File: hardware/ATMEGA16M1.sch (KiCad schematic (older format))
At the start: 56 parts, among them IC1 ATMEGA16M1-A, IC2 MCP2551-I/SN, J1 PWR, J2 USB, J3 RELAY, J4 RELAY, J5 RELAY, J6 GPIO, J7 AMP/D2A, J8 ADC, J9 CAN, SW1 RESET, U1 NCP1117ST50T3G, U2 FT232RL, U3 RELAY_VO14642AT, U4 RELAY_VO14642AT, U5 RELAY_VO14642AT, X1 16MHz

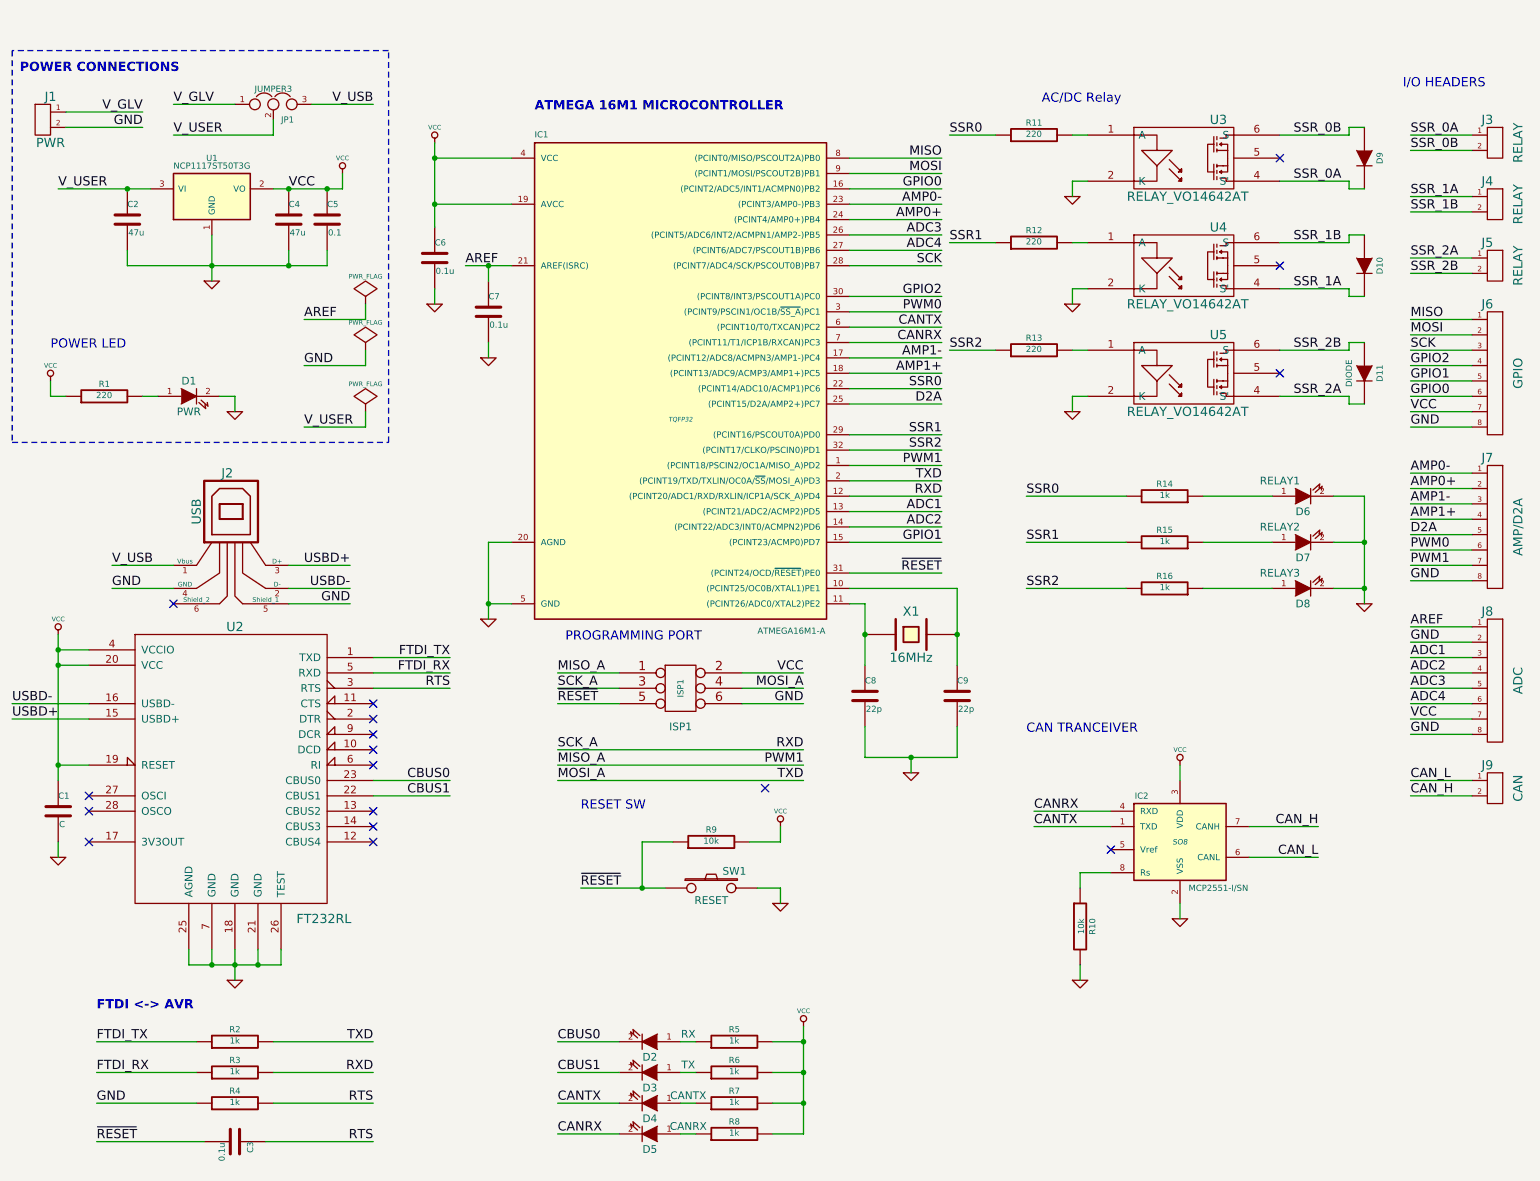
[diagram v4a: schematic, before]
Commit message: BOM added & schematic updated with Digikey P/N's
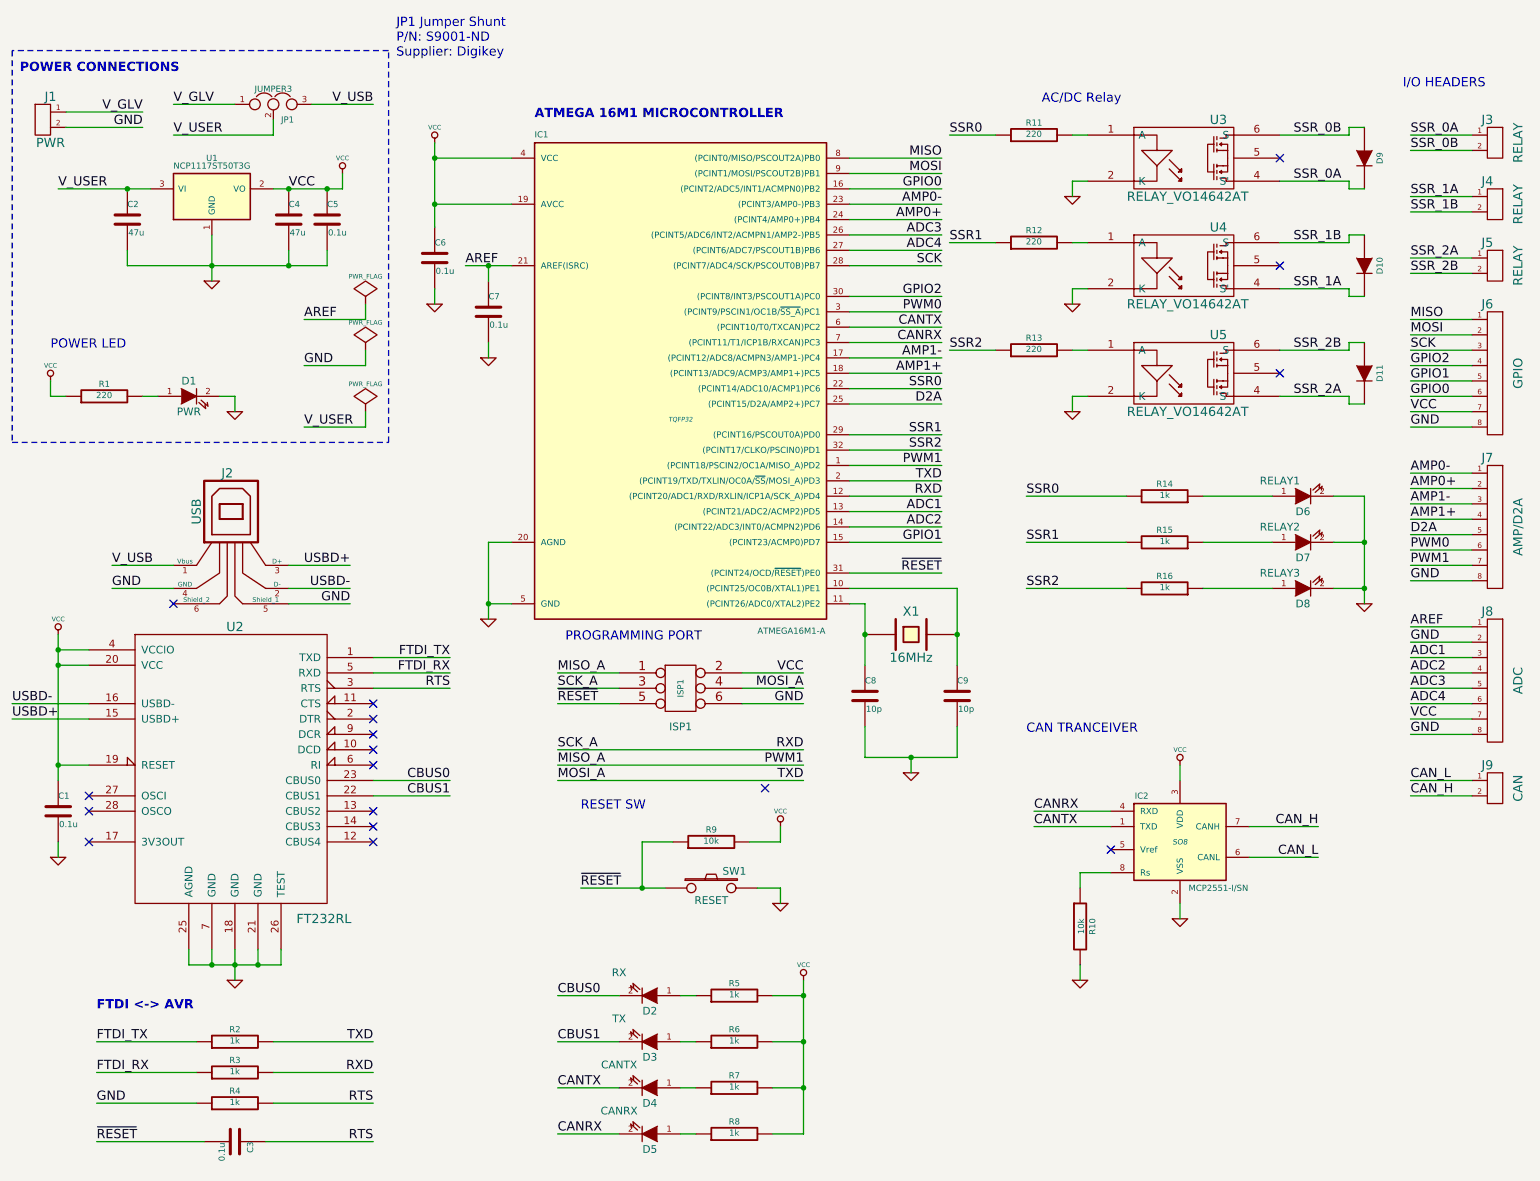
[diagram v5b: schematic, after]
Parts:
- C1: value C -> 0.1u; P/N (none) -> 490-1524-1-ND; Supplier (none) -> Digikey; URL (none) -> http://www.digikey.com/product-detail/en/GRM188R71E104KA01D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
- C2, C4: P/N (none) -> PCE5005CT-ND; Supplier (none) -> Digikey; URL (none) -> http://www.digikey.com/product-detail/en/EEE-FT1E470AR/PCE5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
- C3, C6, C7: P/N (none) -> 490-1524-1-ND; Supplier (none) -> Digikey; URL (none) -> http://www.digikey.com/product-detail/en/GRM188R71E104KA01D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
- C5: value 0.1 -> 0.1u; P/N (none) -> 490-1524-1-ND; Supplier (none) -> Digikey; URL (none) -> http://www.digikey.com/product-detail/en/GRM188R71E104KA01D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
- C8, C9: value 22p -> 10p; P/N (none) -> 490-1403-1-ND; Supplier (none) -> Digikey; URL (none) -> http://www.digikey.com/product-detail/en/GRM1885C1H100JA01D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
- D10, D11, D9: P/N (none) -> SK310A-LTPMSCT-ND; Supplier (none) -> Digikey; URL (none) -> http://www.digikey.com/product-detail/en/SK310A-LTP/SK310A-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
- D2, D5: P/N (none) -> 732-4981-1-ND; Supplier (none) -> Digikey; URL (none) -> http://www.digikey.com/product-detail/en/150060YS75000/732-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
- D3, D4: P/N (none) -> 732-4978-1-ND; Supplier (none) -> Digikey; URL (none) -> http://www.digikey.com/product-detail/en/150060RS75000/732-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
- D6, D7, D8: P/N (none) -> 732-4971-1-ND; Supplier (none) -> Digikey; URL (none) -> http://www.digikey.com/product-detail/en/150060GS75000/732-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
- IC2: P/N (none) -> MCP2551T-E/SNCT-ND; Supplier (none) -> Digikey; URL (none) -> http://www.digikey.com/product-detail/en/MCP2551T-E%2FSN/MC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
- ISP1: P/N (none) -> 3M15451-ND; Supplier (none) -> Digikey; URL (none) -> http://www.digikey.com/product-detail/en/30306-6002HB/3M154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
- J1, J3, J4, J5, J9: P/N (none) -> ED2609-ND; Supplier (none) -> Digikey; URL (none) -> http://www.digikey.com/product-detail/en/OSTTC022162/ED2609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
- J2: P/N (none) -> 609-4613-1-ND; Supplier (none) -> Digikey; URL (none) -> http://www.digikey.com/product-detail/en/10118192-0001LF/60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
- J6, J7, J8: P/N (none) -> ED2615-ND; Supplier (none) -> Digikey; URL (none) -> http://www.digikey.com/product-detail/en/OSTTC082162/ED2615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
- JP1: P/N (none) -> 952-2264-ND; Supplier (none) -> Digikey; URL (none) -> http://www.digikey.com/product-detail/en/M20-9990346/952-22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
- R1, R11, R12, R13: P/N (none) -> RHM220CGCT-ND; Supplier (none) -> Digikey; URL (none) -> http://www.digikey.com/product-detail/en/MCR03ERTJ221/RHM22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
- R10, R9: P/N (none) -> RHM10KCGCT-ND; Supplier (none) -> Digikey; URL (none) -> http://www.digikey.com/product-detail/en/MCR03ERTJ103/RHM10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
- R14, R15, R16, R2, R3, R4, R5, R6, R7, R8: P/N (none) -> RHM1.0KCGCT-ND; Supplier (none) -> Digikey; URL (none) -> http://www.digikey.com/product-detail/en/MCR03ERTJ102/RHM1.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
- SW1: P/N (none) -> 401-1427-1-ND; Supplier (none) -> Digikey; URL (none) -> http://www.digikey.com/product-detail/en/KMR221GLFS/401-142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
- U2: footprint (none) -> ~; P/N (none) -> 768-1007-1-ND; Supplier (none) -> Digikey; URL (none) -> http://www.digikey.com/product-detail/en/FT232RL-REEL/768-1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
- U3: P/N (none) -> VO14642AABCT-ND; Supplier (none) -> Digkey; URL (none) -> http://www.digikey.com/product-detail/en/VO14642AABTR/VO146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
- U4, U5: P/N (none) -> VO14642AABCT-ND; Supplier (none) -> Digikey; URL (none) -> http://www.digikey.com/product-detail/en/VO14642AABTR/VO146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
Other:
- note added: "JP1 Jumper Shunt\nP/N: S9001-ND\nSupplier: Digikey"
- moved on the sheet: D2, D3, D4, R5, R6, R7

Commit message: FTDI <-> ISP issue addressed, dip switch added
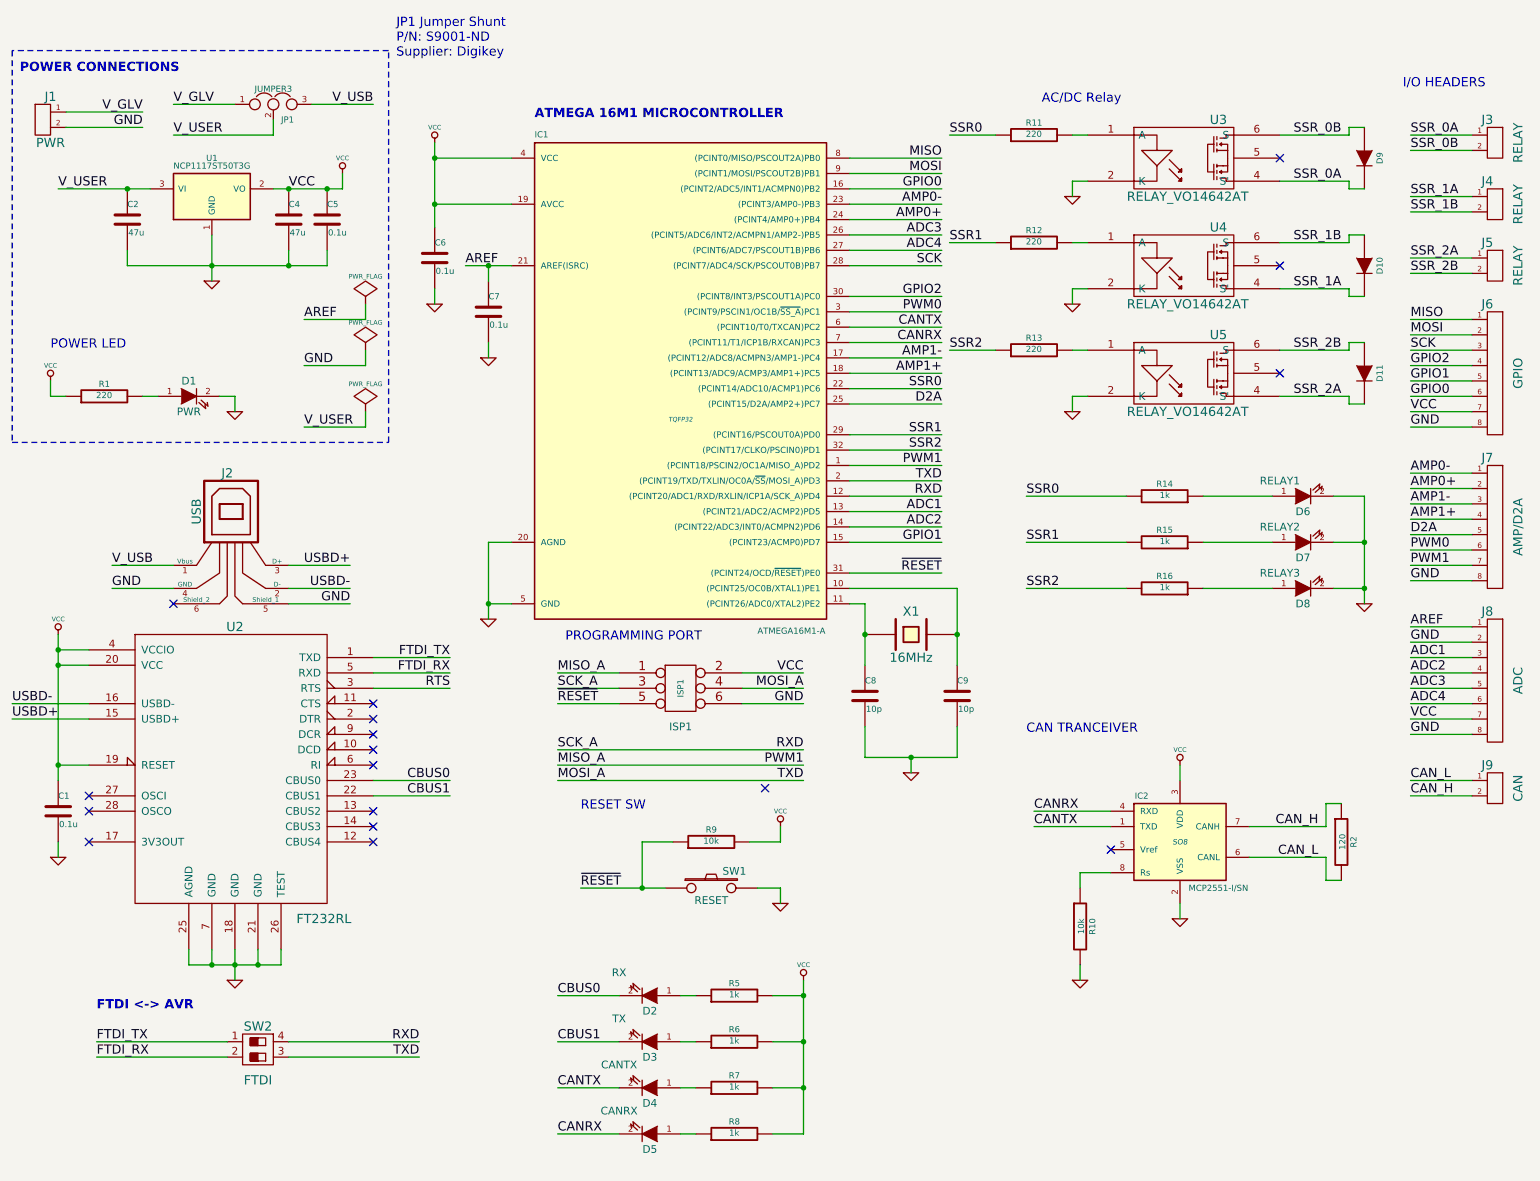
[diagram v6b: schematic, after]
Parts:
- removed C3: 0.1u, ~, symbol C
- removed R3, R4: 1k, ~, symbol R
- added SW2: FTDI, symbol DIPS_02
- R2: value 1k -> 120; P/N RHM1.0KCGCT-ND -> (none); Supplier Digikey -> (none); URL http://www.digikey.com/product-detail/en/MCR03ERTJ102/RHM1.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 -> (none)
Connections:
- net CAN_H: now also R2.1
- net CAN_L: now also R2.2
- net FTDI_RX: now also SW2.2
- net FTDI_TX: now also SW2.1; no longer R2.1
- net MOSI_A: now also SW2.3; no longer R2.2
- net RXD: now also SW2.4
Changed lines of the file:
@@
 LIBS:w_analog
 LIBS:custom
+LIBS:dips-s
 LIBS:ATMEGA16M1-cache
 EELAYER 27 0
@@
 Sheet 1 1
 Title "LFEF CAN Communication Board"
-Date "2 apr 2015"
+Date "11 apr 2015"
 Rev "0"
 Comp "Lafayette College"
@@
 	1    0    0    -1
 $EndComp
-Text Label 2900 7000 2    60   ~ 0
+Text Label 3200 7100 2    60   ~ 0
 TXD
-Text Label 2900 7200 2    60   ~ 0
+Text Label 3200 7000 2    60   ~ 0
 RXD
-$Comp
-L R R2
-U 1 1 54DE18B6
-P 2000 7000
-F 0 "R2" V 2080 7000 40  0000 C CNN
-F 1 "1k" V 2007 7001 40  0000 C CNN
-F 2 "~" V 1930 7000 30  0000 C CNN
-F 3 "~" H 2000 7000 30  0000 C CNN
-F 4 "RHM1.0KCGCT-ND" H 2000 7000 60  0001 C CNN "P/N"
-F 5 "Digikey" H 2000 7000 60  0001 C CNN "Supplier"
-F 6 "http://www.digikey.com/product-detail/en/MCR03ERTJ102/RHM1.0KCGCT-ND/2796495" H 2000 7000 60  0001 C CNN "URL"
-	1    2000 7000
-	0    -1   -1   0
-$EndComp
-$Comp
-L R R3
-U 1 1 54DE18C3
-P 2000 7200
-F 0 "R3" V 2080 7200 40  0000 C CNN
-F 1 "1k" V 2007 7201 40  0000 C CNN
-F 2 "~" V 1930 7200 30  0000 C CNN
-F 3 "~" H 2000 7200 30  0000 C CNN
-F 4 "RHM1.0KCGCT-ND" H 2000 7200 60  0001 C CNN "P/N"
-F 5 "Digikey" H 2000 7200 60  0001 C CNN "Supplier"
-F 6 "http://www.digikey.com/product-detail/en/MCR03ERTJ102/RHM1.0KCGCT-ND/2796495" H 2000 7200 60  0001 C CNN "URL"
-	1    2000 7200
-	0    -1   -1   0
-$EndComp
 Text Label 1100 7000 0    60   ~ 0
 FTDI_TX
-Text Label 1100 7200 0    60   ~ 0
+Text Label 1100 7100 0    60   ~ 0
 FTDI_RX
-Text Label 2900 7650 2    60   ~ 0
-RTS
-Text Label 1100 7650 0    60   ~ 0
-~RESET
-$Comp
-L C C3
-U 1 1 54DE18FF
-P 2000 7650
-F 0 "C3" H 2000 7750 40  0000 L CNN
-F 1 "0.1u" H 2006 7565 40  0000 L CNN
-F 2 "~" H 2038 7500 30  0000 C CNN
-F 3 "~" H 2000 7650 60  0000 C CNN
-F 4 "490-1524-1-ND" H 2000 7650 60  0001 C CNN "P/N"
-F 5 "Digikey" H 2000 7650 60  0001 C CNN "Supplier"
-F 6 "http://www.digikey.com/product-detail/en/GRM188R71E104KA01D/490-1524-1-ND/587865" H 2000 7650 60  0001 C CNN "URL"
-	1    2000 7650
-	0    1    1    0
-$EndComp
 $Comp
 L C C5
@@
 Text Notes 3950 1000 0    60   ~ 12
 ATMEGA 16M1 MICROCONTROLLER
-Text Label 2900 7400 2    60   ~ 0
-RTS
-$Comp
-L R R4
-U 1 1 54DE1D1D
-P 2000 7400
-F 0 "R4" V 2080 7400 40  0000 C CNN
-F 1 "1k" V 2007 7401 40  0000 C CNN
-F 2 "~" V 1930 7400 30  0000 C CNN
-F 3 "~" H 2000 7400 30  0000 C CNN
-F 4 "RHM1.0KCGCT-ND" H 2000 7400 60  0001 C CNN "P/N"
-F 5 "Digikey" H 2000 7400 60  0001 C CNN "Supplier"
-F 6 "http://www.digikey.com/product-detail/en/MCR03ERTJ102/RHM1.0KCGCT-ND/2796495" H 2000 7400 60  0001 C CNN "URL"
-	1    2000 7400
-	0    -1   -1   0
-$EndComp
-Text Label 1100 7400 0    60   ~ 0
-GND
 $Comp
 L MCP2551-I/SN IC2
@@
 	3800 4150 3650 4150
 Wire Wire Line
-	3650 3750 3650 4150
-Wire Wire Line
-	3650 4150 3650 4250
+	3650 3750 3650 4250
 Wire Wire Line
 	3800 1250 3300 1250
 Wire Wire Line
-	3300 1150 3300 1250
-Wire Wire Line
-	3300 1250 3300 1550
-Wire Wire Line
-	3300 1550 3300 1700
+	3300 1150 3300 1700
 Wire Wire Line
 	6000 4150 6100 4150
 Wire Wire Line
-	6100 4150 6100 4350
-Wire Wire Line
-	6100 4350 6100 4550
+	6100 4150 6100 4550
 Wire Wire Line
 	6000 4050 6700 4050
 Wire Wire Line
-	6700 4050 6700 4350
-Wire Wire Line
-	6700 4350 6700 4550
+	6700 4050 6700 4550
 Connection ~ 6100 4350
 Connection ~ 6700 4350
@@
 	6100 4950 6100 5150
 Wire Wire Line
-	6100 5150 6400 5150
-Wire Wire Line
-	6400 5150 6700 5150
+	6100 5150 6700 5150
 Wire Wire Line
 	6700 5150 6700 4950
@@
 Connection ~ 3650 4150
 Wire Wire Line
-	3500 1950 3650 1950
-Wire Wire Line
-	3650 1950 3800 1950
-Wire Wire Line
-	1850 1750 1850 1950
-Wire Wire Line
-	1850 1950 1850 2050
+	3500 1950 3800 1950
+Wire Wire Line
+	1850 1750 1850 2050
 Wire Wire Line
 	1300 1850 1300 1950
 Wire Wire Line
-	1300 1950 1850 1950
-Wire Wire Line
-	1850 1950 2350 1950
-Wire Wire Line
-	2350 1950 2600 1950
+	1300 1950 2600 1950
 Connection ~ 1850 1950
 Wire Wire Line
-	2250 1450 2350 1450
-Wire Wire Line
-	2350 1450 2600 1450
-Wire Wire Line
-	2600 1450 2700 1450
-Wire Wire Line
-	850  1450 1300 1450
-Wire Wire Line
-	1300 1450 1450 1450
+	2250 1450 2700 1450
+Wire Wire Line
+	850  1450 1450 1450
 Wire Wire Line
 	2350 1950 2350 1850
@@
 	3300 2100 3300 2200
 Wire Wire Line
-	2900 7000 2250 7000
-Wire Wire Line
-	2900 7200 2250 7200
-Wire Wire Line
-	1100 7000 1750 7000
-Wire Wire Line
-	1100 7200 1750 7200
-Wire Wire Line
-	2900 7650 2200 7650
-Wire Wire Line
-	1100 7650 1800 7650
+	3200 7000 2350 7000
+Wire Wire Line
+	3200 7100 2350 7100
+Wire Wire Line
+	1100 7000 1950 7000
+Wire Wire Line
+	1100 7100 1950 7100
 Connection ~ 2600 1450
 Wire Wire Line
@@
 	3000 550  550  550
 Wire Wire Line
-	2900 7400 2250 7400
-Wire Wire Line
-	1100 7400 1750 7400
-Wire Wire Line
-	8600 5600 9050 5600
-Wire Wire Line
-	8600 5800 9050 5800
+	8600 5600 9100 5600
+Wire Wire Line
+	8600 5800 9100 5800
 Wire Wire Line
 	7700 5500 7200 5500
@@
 	1850 6400 1850 6500
 Wire Wire Line
-	2000 6400 2000 6500
-Wire Wire Line
-	2000 6500 2000 6600
+	2000 6400 2000 6600
 Wire Wire Line
 	2150 6500 2150 6400
 Wire Wire Line
-	1700 6500 1850 6500
-Wire Wire Line
-	1850 6500 2000 6500
-Wire Wire Line
-	2000 6500 2150 6500
-Wire Wire Line
-	2150 6500 2300 6500
+	1700 6500 2300 6500
 Connection ~ 1850 6500
 Connection ~ 2000 6500
@@
 	850  4550 1050 4550
 Wire Wire Line
-	850  4350 850  4450
-Wire Wire Line
-	850  4450 850  4550
-Wire Wire Line
-	850  4550 850  5200
-Wire Wire Line
-	850  5200 850  5300
+	850  4350 850  5300
 Wire Wire Line
 	1050 4450 850  4450
@@
 	9350 3750 9150 3750
 Wire Wire Line
-	5700 6600 5700 7000
-Wire Wire Line
-	5700 7000 5700 7300
-Wire Wire Line
-	5700 7300 5700 7600
+	5700 6600 5700 7600
 Wire Wire Line
 	5700 7000 5500 7000
@@
 	5550 5700 5550 5600
 Wire Wire Line
-	4250 6000 4650 6000
-Wire Wire Line
-	4650 6000 4800 6000
+	4250 6000 4800 6000
 Wire Wire Line
 	4650 6000 4650 5700
@@
 	9350 4050 9150 4050
 Wire Wire Line
-	9350 3450 9350 3750
-Wire Wire Line
-	9350 3750 9350 4050
-Wire Wire Line
-	9350 4050 9350 4150
+	9350 3450 9350 4150
 Connection ~ 9350 3750
 Connection ~ 9350 4050
@@
 Text Notes 3050 600  0    60   ~ 0
 JP1 Jumper Shunt\nP/N: S9001-ND\nSupplier: Digikey
+$Comp
+L R R2
+U 1 1 55284A3E
+P 9200 5700
+F 0 "R2" V 9280 5700 40  0000 C CNN
+F 1 "120" V 9207 5701 40  0000 C CNN
+F 2 "~" V 9130 5700 30  0000 C CNN
+F 3 "~" H 9200 5700 30  0000 C CNN
+	1    9200 5700
+	1    0    0    -1
+$EndComp
+Wire Wire Line
+	9100 5600 9100 5450
+Wire Wire Line
+	9100 5450 9200 5450
+Wire Wire Line
+	9100 5800 9100 5950
+Wire Wire Line
+	9100 5950 9200 5950
+$Comp
+L DIPS_02 SW2
+U 1 1 55287F34
+P 2150 7050
+F 0 "SW2" V 2000 7050 60  0000 C CNN
+F 1 "FTDI" V 2350 7050 60  0000 C CNN
+F 2 "" H 2150 7050 60  0000 C CNN
+F 3 "" H 2150 7050 60  0000 C CNN
+	1    2150 7050
+	0    1    1    0
+$EndComp
 $EndSCHEMATC

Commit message: Reference designations updated, BOM.csv reflects changes & RTS DTR added
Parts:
- added R2, R3: 100, ~, symbol R
- renumbered C4 to C3, C5 to C4, C6 to C5, C7 to C6, C8 to C7, C9 to C8, R12 to R10, R13 to R11, R10 to R12, R14 to R13, R15 to R14, R16 to R15, R2 to R16, R9 to R4, R11 to R9, IC1 to U3, IC2 to U4, U3 to U5, U4 to U6, U5 to U7
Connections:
- net CANRX: now also R8.1; no longer D5.2 (K)
- net CANTX: now also R7.1; no longer D4.2 (K)
- net GND: now also D4.2 (K), D5.2 (K)
- net RTS: now also R2.1
- net VCC: no longer R7.2, R8.2
- net ~RESET: now also R2.2, R3.2
- net DTR: now reaches U2.2 (DTR)
- net DTR: now also R3.1
- net at D4.1 (A): now also R7.2; no longer R7.1
- net at D5.1 (A): now also R8.2; no longer R8.1
- no-connect marks 17 -> 16
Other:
- moved on the sheet: D4, D5, R7, R8
